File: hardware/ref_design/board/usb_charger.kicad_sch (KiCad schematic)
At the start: 20 parts, among them J1 TYPE-C-31-M-12, J2 S2B-PH-SM4-TB, U1 USBLC6-2SC6, U2 BQ24074RGTR

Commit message: Reference design: case, board pipeline, routing tools and docs
- case/case.scad now owns every position the board needs (outline,
  cable slot, contacts, screws, USB-C, power button, pinholes, light
  pipes, height limits) and exports them to positions.json; tub, lid
  and power cap STLs, lens and board outlines as DXF.
- board/placement.py + tools/build_pcb.py: a 4-layer board built from
  KiCad's netlist with pcbnew, every footprint linked to its symbol
  (DRC schematic parity: 0), the RP2350B core's placement, routing and
  regulator copper copied from Raspberry Pi's minimal design.
- tools/route.py: planes, pre-routes the autorouter can't do (membrane
  combs, the display's grounded RGB pins, plane fan-out), Freerouting
  1.9 on a corrected copy of the board, pours, stitching, repair.
- Footprint copies that carry vendor 3D models (USB-C, JST, switches)
  checked against their pads; speaker pads moved to the back as SMD;
  the Alps switch's pads pulled back from its locating holes.
- docs: README, assembly, bring-up, pin map (generated), BOM, design
  review, and the Konnect problems met on the way.

Co-Authored-By: Claude Opus 5.5 (1M context) <noreply@anthropic.com>
Claude-Session: https://claude.ai/code/session_01KGgEu3CbFtCsvHRQgAFiCN
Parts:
- J1: footprint Connector_USB:USB_C_Receptacle_HRO_TYPE-C-31-M-12 -> battler:USB_C_Receptacle_HRO_TYPE-C-31-M-12
- J2: footprint Connector_JST:JST_PH_S2B-PH-SM4-TB_1x02-1MP_P2.00mm_Horizontal -> battler:JST_PH_S2B-PH-SM4-TB_1x02-1MP_P2.00mm_Horizontal
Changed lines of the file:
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@@
         (font
           (size 1.27 1.27))))
-    (property "Footprint" "Connector_USB:USB_C_Receptacle_HRO_TYPE-C-31-M-12"
+    (property "Footprint" "battler:USB_C_Receptacle_HRO_TYPE-C-31-M-12"
       (at 25.4 40.64 0)
       (effects
@@
         (font
           (size 1.27 1.27))))
-    (property "Footprint" "Connector_JST:JST_PH_S2B-PH-SM4-TB_1x02-1MP_P2.00mm_Horizontal"
+    (property "Footprint" "battler:JST_PH_S2B-PH-SM4-TB_1x02-1MP_P2.00mm_Horizontal"
       (at 218.44 119.38 0)
       (effects

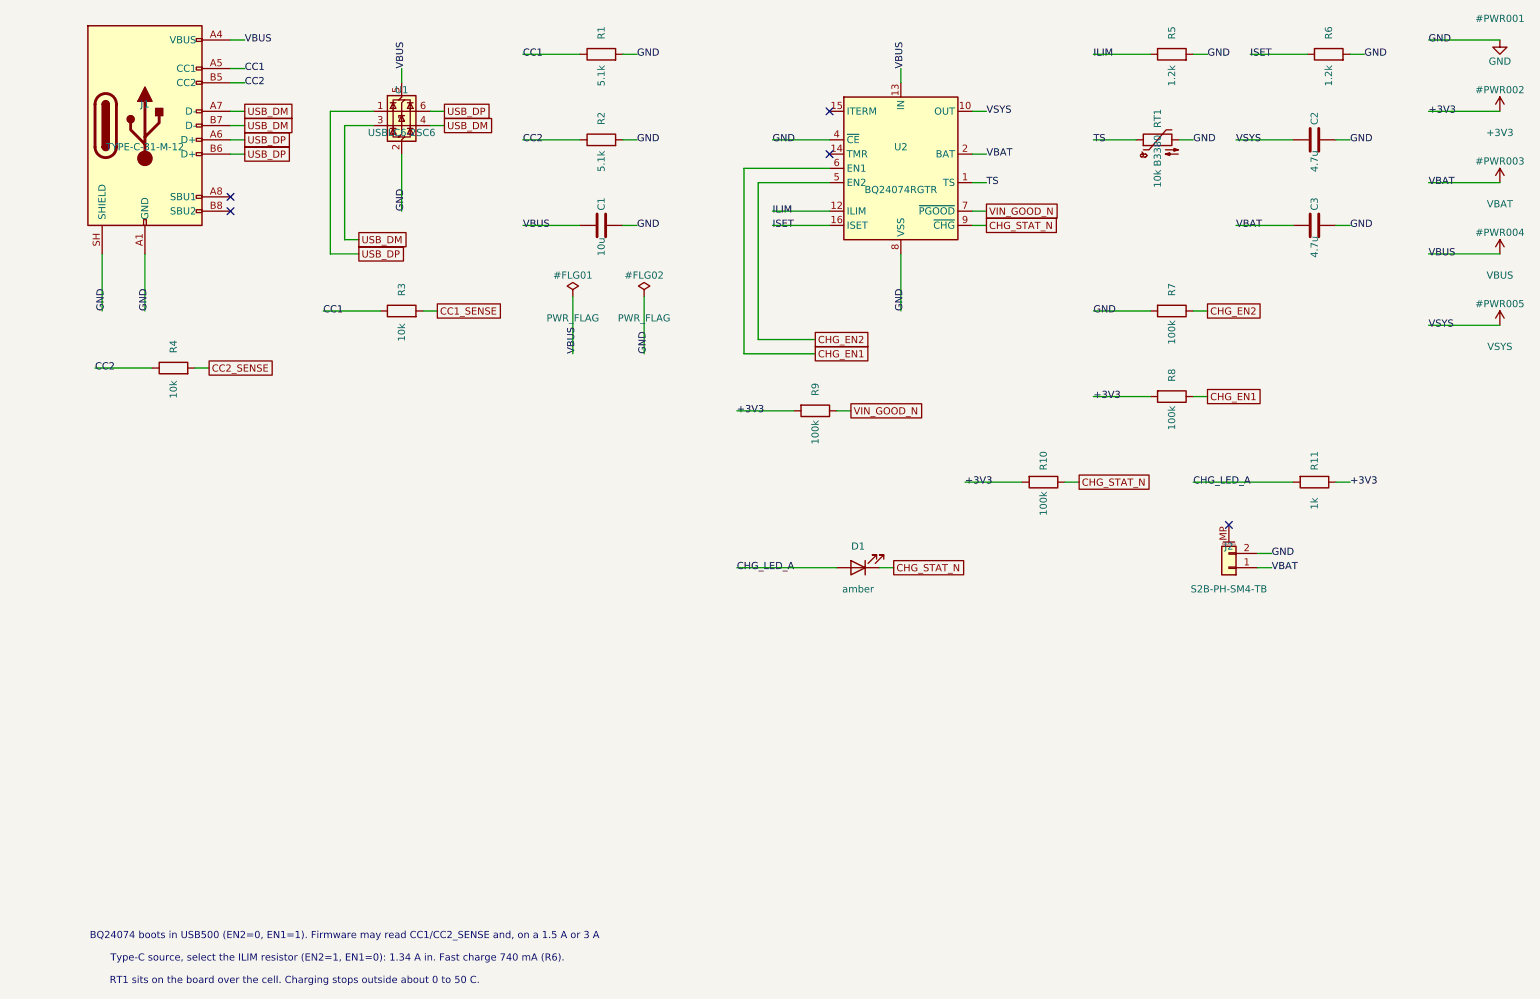
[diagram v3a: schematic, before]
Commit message: 2-layer fork: approved circuit changes in the design data and schematic
TP4056 charger (500 mA, TEMP grounded) with USB load sharing (B5819W, AO3401A
gate fed through a BAT54WS so it switches at once on an unplug, 22 uF on VSYS),
ME6211 3V3 LDO on the power latch, RP2354B with its flash inside (only the
QSPI_SS strap outside), 27 ohm 0603 USB resistors, SRV05-4 ESD, PWM audio
through two RC poles into an FM8002A, seat 1's Y contact as the power button,
no LEDs, no thermistor. Thermal-via footprints use 0.3 mm holes. Netlist
check passes, ERC 0 errors.

Co-Authored-By: Claude Opus 5.5 <noreply@anthropic.com>
Claude-Session: https://claude.ai/code/session_01KGgEu3CbFtCsvHRQgAFiCN
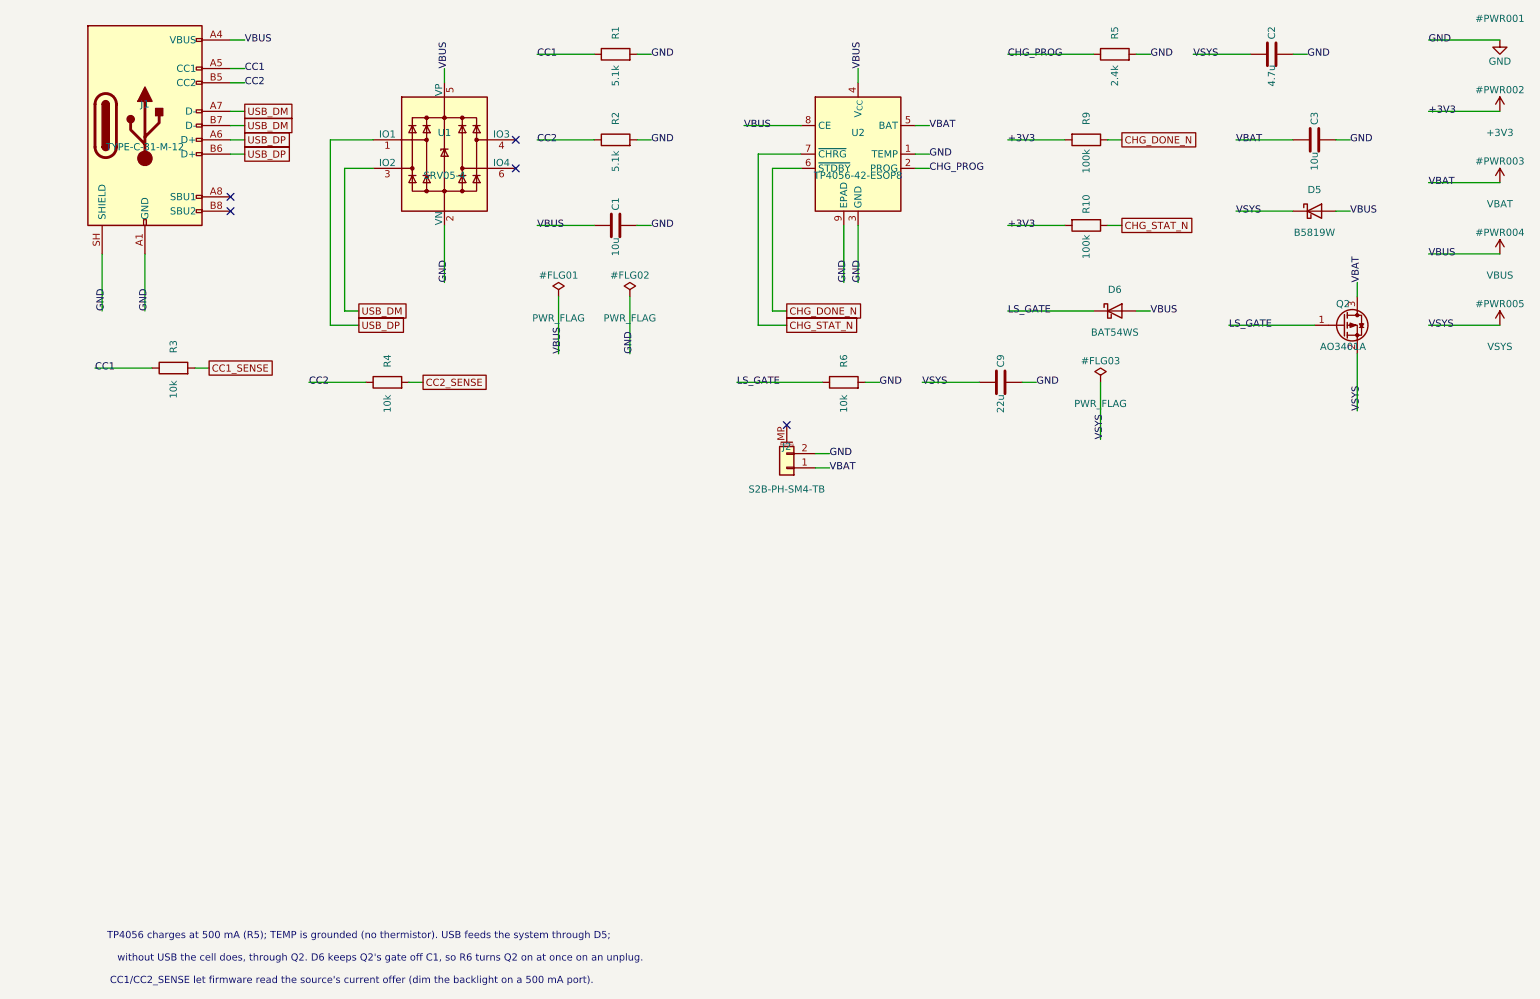
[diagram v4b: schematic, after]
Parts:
- removed D1: amber, LED_SMD:LED_0603_1608Metric, symbol Device:LED
- removed R11: 1k, Resistor_SMD:R_0402_1005Metric, symbol Device:R
- removed R7, R8: 100k, Resistor_SMD:R_0402_1005Metric, symbol Device:R
- removed RT1: 10k B3380, Resistor_SMD:R_0603_1608Metric, symbol Device:Thermistor_NTC
- removed U1: USBLC6-2SC6, Package_TO_SOT_SMD:SOT-23-6, symbol Power_Protection:USBLC6-2P6
- removed U2: BQ24074RGTR, Package_DFN_QFN:VQFN-16-1EP_3x3mm_P0.5mm_EP1.6x1.6mm_ThermalVias, symbol Battery_Management:BQ24074RGT
- added C9: 22u, Capacitor_SMD:C_0805_2012Metric, symbol Device:C
- added D5: B5819W, Diode_SMD:D_SOD-123, symbol Device:D_Schottky
- added D6: BAT54WS, Diode_SMD:D_SOD-323, symbol Device:D_Schottky
- added Q2: AO3401A, Package_TO_SOT_SMD:SOT-23, symbol Transistor_FET:Q_PMOS_GSD
- added U1: SRV05-4, Package_TO_SOT_SMD:SOT-23-6, symbol Power_Protection:SRV05-4
- added U2: TP4056-42-ESOP8, battler:SOIC-8-1EP_3.9x4.9mm_P1.27mm_EP2.41x3.3mm_ThermalVias_0.3mm, symbol Battery_Management:TP4056-42-ESOP8
- C3: value 4.7u -> 10u; LCSC C19666 -> C19702; MPN CL10A475KO8NNNC -> CL10A106KP8NNNC
- R5: value 1.2k -> 2.4k; LCSC C25862 -> C25882; MPN 0402WGF1201TCE -> 0402WGF2401TCE
- R6: value 1.2k -> 10k; LCSC C25862 -> C25744; MPN 0402WGF1201TCE -> 0402WGF1002TCE
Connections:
- net CHG_STAT_N: now also U2.7 (~{CHRG})
- net GND: now also C9.2, U1.2 (VN), U2.1 (TEMP), U2.3 (GND), U2.9 (EPAD)
- net USB_DM: now also U1.3 (IO2)
- net USB_DP: now also U1.1 (IO1)
- net VBAT: now also Q2.3 (D), U2.5 (BAT)
- net VBUS: now also D5.2 (A), D6.2 (A), U1.5 (VP), U2.4 (V_{CC}), U2.8 (CE)
- net VSYS: now also C9.1, D5.1 (K), Q2.2 (S)
- net ILIM renamed CHG_PROG
- net CHG_PROG: now also U2.2 (PROG)
- net ISET renamed LS_GATE
- net LS_GATE: now also D6.1 (K), Q2.1 (G)
- net VIN_GOOD_N renamed CHG_DONE_N
- net CHG_DONE_N: now also U2.6 (~{STDBY})
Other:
- note added: "CC1/CC2_SENSE let firmware read the source's current offer (dim the backlight on a 500 mA port)."
- note added: "TP4056 charges at 500 mA (R5); TEMP is grounded (no thermistor). USB feeds the system through D5;"
- note added: "without USB the cell does, through Q2. D6 keeps Q2's gate off C1, so R6 turns Q2 on at once on an unplug."
- note removed: "BQ24074 boots in USB500 (EN2=0, EN1=1). Firmware may read CC1/CC2_SENSE and, on a 1.5 A or 3 A"
- note removed: "RT1 sits on the board over the cell. Charging stops outside about 0 to 50 C."
- note removed: "Type-C source, select the ILIM resistor (EN2=1, EN1=0): 1.34 A in. Fast charge 740 mA (R6)."

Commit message: Reference design: audit round 1 fixes (USB ESD reference, PWR_EN pull-down)
From an independent audit of the 2-layer board:
- SRV05-4 REF (U1 pin 5) moves from VBUS to 3V3. On VBUS, with no cable in,
  the MCU's D+ pull-up (always on in BOOTSEL mode) fed VBUS through the D+
  steering diode to about 2.7 V: PWR_EN stayed up, so the device could not
  turn off, and the load-sharing FET was left half on.
- R15 (PWR_EN pull-down) 100k -> 10k, so D5's reverse leakage into the VBUS
  node can't lift the ME6211's CE to 1.0 V when warm.
- J6 (UART) turned 180 degrees: its mouth faced J5's back 5 mm away.
- Lid: the panel's locating frame gets 0.8 mm clearance (panel_fit), not 0.4.
- Docs: ILI9488 reads at 5 MHz or less, TP4056 current 460-500 mA and its
  145 C thermal limit, how 3V3 reaches the core pour, FPC insertion depth and
  expected slack, JLC's 374 solder joints, board size as quoted.

Checks: netlist PASS, ERC 0, DRC 0 errors / 0 unconnected / 0 parity
(2 cosmetic silk warnings), fit PASS on 91 parts.

Co-Authored-By: Claude Opus 5.5 <noreply@anthropic.com>
Claude-Session: https://claude.ai/code/session_01KGgEu3CbFtCsvHRQgAFiCN
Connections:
- net +3V3: now also U1.5 (VP)
- net VBUS: no longer U1.5 (VP)
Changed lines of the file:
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@@
     (at 54.61 86.36 0)
 )
-  (label "VBUS"
+  (label "+3V3"
     (at 78.74 30.48 90)
 )

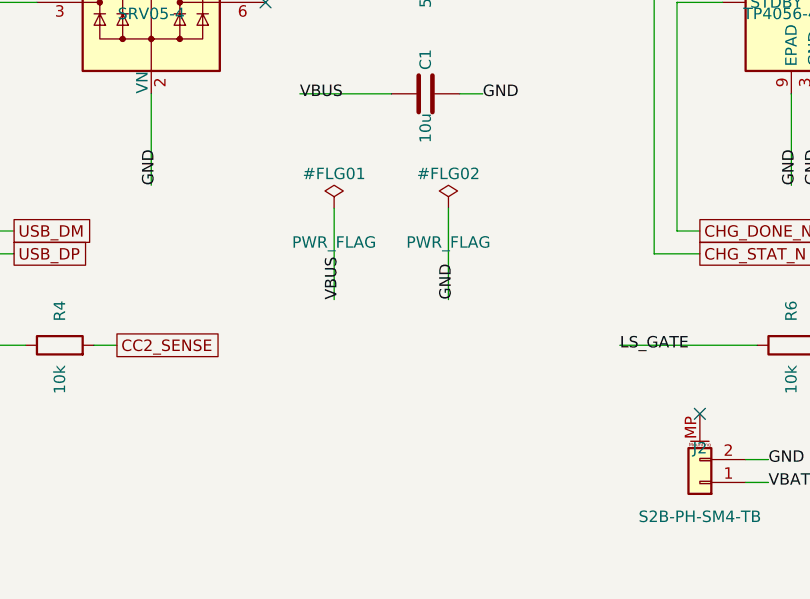
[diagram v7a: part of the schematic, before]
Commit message: Reference design: audit round 2 fixes (VBUS bleeder, window, fit check)
- R15 back to 100k and a 10k VBUS bleeder (R38) instead: the 10k R15 cut the
  Y contact's pill-resistance margin for Q1 about five times. The bleeder
  needs about 140 uA of D5 leakage before CE reaches 1.0 V; 0.5 mA on USB.
  R38 sits beside R14 (next to C1 it blocked seat 1's A route).
- Lid window margin 0.5 -> 0.8 mm: covers the panel's +-0.4 float in its
  frame and its +-0.3 active-area tolerance. Frame wall and depth named.
- check_fit.py knows the lid's panel frame: parts under its band are held
  to its lower limit (3.6 mm).
- route.py: the final cleanup also drops a pour's via that joins nothing
  (a stitching via left in a pocket the pours never reached).

Checks: netlist PASS (123 parts), ERC 0, DRC 0 errors / 0 unconnected /
0 parity (2 cosmetic silk warnings), fit PASS on 92 parts.

Co-Authored-By: Claude Opus 5.5 <noreply@anthropic.com>
Claude-Session: https://claude.ai/code/session_01KGgEu3CbFtCsvHRQgAFiCN
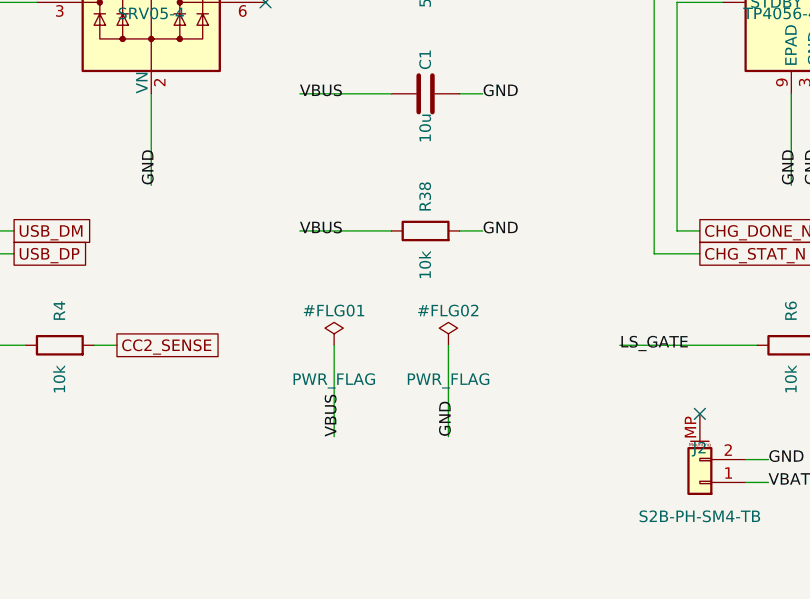
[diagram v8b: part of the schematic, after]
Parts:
- added R38: 10k, Resistor_SMD:R_0402_1005Metric, symbol Device:R
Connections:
- net GND: now also R38.2
- net VBUS: now also R38.1
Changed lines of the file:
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@@
+  (wire
+    (pts
+      (xy 105.41 73.66)
+      (xy 95.25 73.66))
+)
+  (wire
+    (pts
+      (xy 113.03 73.66)
+      (xy 115.57 73.66))
+)
   (wire
     (pts
@@
   (wire
     (pts
-      (xy 99.06 71.12)
-      (xy 99.06 81.28))
-)
-  (wire
-    (pts
-      (xy 111.76 71.12)
-      (xy 111.76 81.28))
+      (xy 99.06 86.36)
+      (xy 99.06 96.52))
+)
+  (wire
+    (pts
+      (xy 111.76 86.36)
+      (xy 111.76 96.52))
 )
   (wire
@@
 )
   (label "VBUS"
+    (at 95.25 73.66 0)
+)
+  (label "GND"
+    (at 115.57 73.66 0)
+)
+  (label "VBUS"
     (at 152.4 30.48 90)
 )
@@
 )
   (label "VBUS"
-    (at 99.06 81.28 90)
-)
-  (label "GND"
-    (at 111.76 81.28 90)
+    (at 99.06 96.52 90)
+)
+  (label "GND"
+    (at 111.76 96.52 90)
 )
   (label "VSYS"
@@
           (unit 1)))))
   (symbol
+    (lib_id "Device:R")
+    (at 109.22 73.66 90)
+    (unit 1)
+    (in_bom yes)
+    (on_board yes)
+    (dnp no)
+    (property "Reference" "R38"
+      (at 109.22 69.85 0)
+      (effects
+        (font
+          (size 1.27 1.27))))
+    (property "Value" "10k"
+      (at 109.22 77.47 0)
+      (effects
+        (font
+          (size 1.27 1.27))))
+    (property "Footprint" "Resistor_SMD:R_0402_1005Metric"
+      (at 109.22 73.66 0)
+      (effects
+        (font
+          (size 1.27 1.27))
+        (hide yes)))
+    (property "Datasheet" ""
+      (at 109.22 73.66 0)
+      (effects
+        (font
+          (size 1.27 1.27))
+        (hide yes)))
+    (property "LCSC" "C25744"
+      (at 0 0 0)
+      (effects
+        (font
+          (size 1.27 1.27))
+        (hide yes)))
+    (property "MPN" "0402WGF1002TCE"
+      (at 0 0 0)
+      (effects
+        (font
+          (size 1.27 1.27))
+        (hide yes)))
+    (property "Manufacturer" "UNI-ROYAL"
+      (at 0 0 0)
+      (effects
+        (font
+          (size 1.27 1.27))
+        (hide yes)))
+    (instances
+      (project ""
+        (path "/"
+          (reference "R38")
+          (unit 1)))))
+  (symbol
     (lib_id "Battery_Management:TP4056-42-ESOP8")
     (at 152.4 45.72 0)
@@
   (symbol
     (lib_id "power:PWR_FLAG")
-    (at 99.06 71.12 0)
+    (at 99.06 86.36 0)
     (unit 1)
     (in_bom yes)
@@
     (dnp no)
     (property "Reference" "#FLG01"
-      (at 99.06 67.31 0)
+      (at 99.06 82.55 0)
       (effects
         (font
           (size 1.27 1.27))))
     (property "Value" "PWR_FLAG"
-      (at 99.06 74.93 0)
+      (at 99.06 90.17 0)
       (effects
         (font
           (size 1.27 1.27))))
     (property "Footprint" ""
-      (at 99.06 71.12 0)
-      (effects
-        (font
-          (size 1.27 1.27))
-        (hide yes)))
-    (property "Datasheet" ""
-      (at 99.06 71.12 0)
+      (at 99.06 86.36 0)
+      (effects
+        (font
+          (size 1.27 1.27))
+        (hide yes)))
+    (property "Datasheet" ""
+      (at 99.06 86.36 0)
       (effects
         (font
@@
   (symbol
     (lib_id "power:PWR_FLAG")
-    (at 111.76 71.12 0)
+    (at 111.76 86.36 0)
     (unit 1)
     (in_bom yes)
@@
     (dnp no)
     (property "Reference" "#FLG02"
-      (at 111.76 67.31 0)
+      (at 111.76 82.55 0)
       (effects
         (font
           (size 1.27 1.27))))
     (property "Value" "PWR_FLAG"
-      (at 111.76 74.93 0)
+      (at 111.76 90.17 0)
       (effects
         (font
           (size 1.27 1.27))))
     (property "Footprint" ""
-      (at 111.76 71.12 0)
-      (effects
-        (font
-          (size 1.27 1.27))
-        (hide yes)))
-    (property "Datasheet" ""
-      (at 111.76 71.12 0)
-      (effects
-        (font
+      (at 111.76 86.36 0)
+      (effects
+        (font
+          (size 1.27 1.27))
+        (hide yes)))
+    (property "Datasheet" ""
+      (at 111.76 86.36 0)
+      (effects
+        (font
